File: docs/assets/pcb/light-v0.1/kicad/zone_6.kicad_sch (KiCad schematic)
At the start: 13 parts, among them J7 ZONE 6, Q116 AO3422, Q117 AO3422, Q118 AO3422

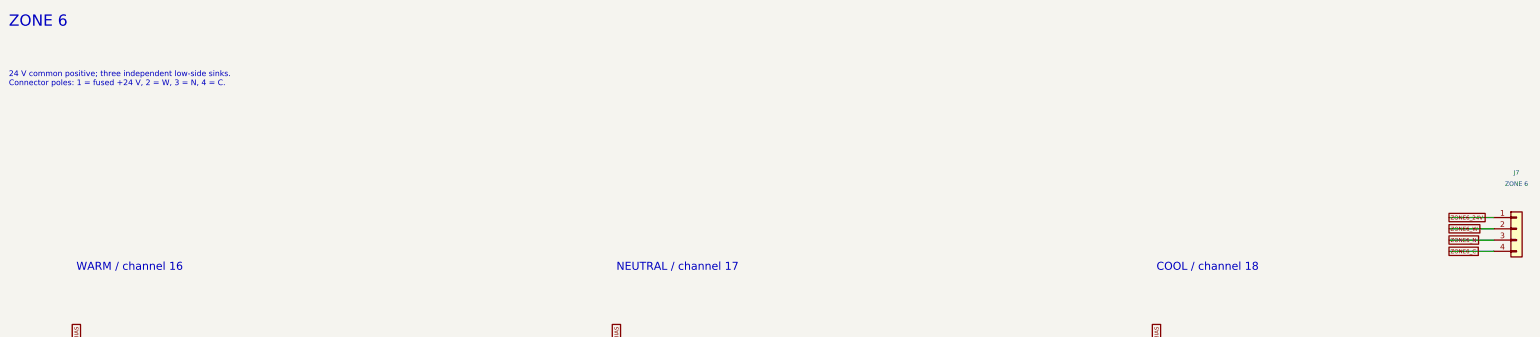
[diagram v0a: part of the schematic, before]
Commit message: Refresh PCB chapters from verified central LED snapshots
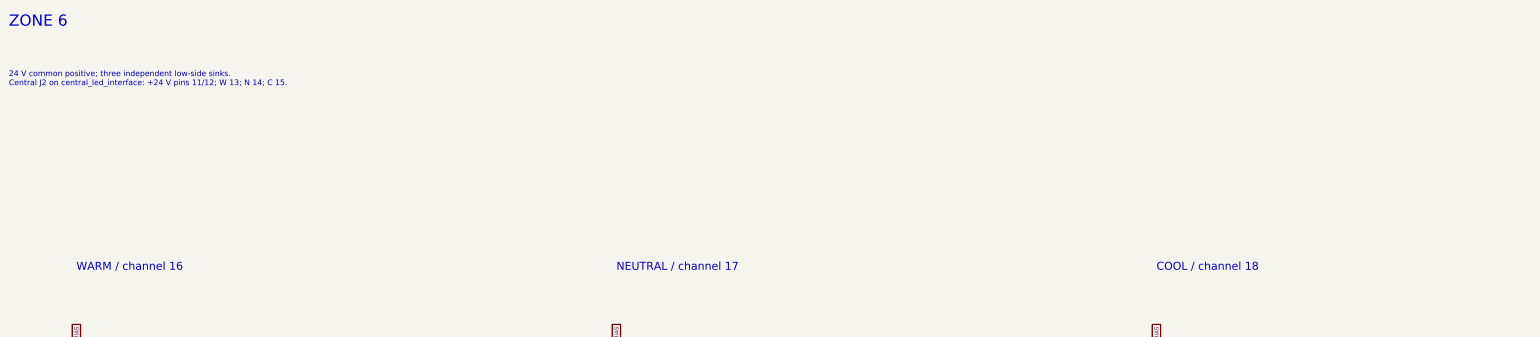
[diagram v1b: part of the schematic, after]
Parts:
- removed J7: ZONE 6, Connector_JST:JST_GH_SM04B-GHS-TB_1x04-1MP_P1.25mm_Horizontal, symbol Connector_Generic:Conn_01x04
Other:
- note added: "24 V common positive; three independent low-side sinks. Central J2 on central_led_interface: +24 V pins 11/12; W 13; N 14; C 15."
- note removed: "24 V common positive; three independent low-side sinks. Connector poles: 1 = fused +24 V, 2 = W, 3 = N, 4 = C."
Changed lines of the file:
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@@
   (title_block
     (title "Zone 6")
-    (date "2026-09-06")
-    (rev "A draft")
+    (date "2026-09-08")
+    (rev "LIGHT v0.2 candidate")
     (company "Engineered Lighting")
     (comment 1 "ENGINEERING DRAFT - see release status before fabrication"))
-  (symbol
-    (lib_id "Connector_Generic:Conn_01x04")
-    (at 360.68 63.5 0)
-    (unit 1)
-    (exclude_from_sim yes)
-    (in_bom yes)
-    (on_board yes)
-    (dnp no)
-    (property "Reference" "J7"
-      (at 360.68 50.8 0.0)
-      (effects
-        (font
-          (size 1.0 1.0))))
-    (property "Value" "ZONE 6"
-      (at 360.68 53.34 0.0)
-      (effects
-        (font
-          (size 1.0 1.0))))
-    (property "Footprint" "Connector_JST:JST_GH_SM04B-GHS-TB_1x04-1MP_P1.25mm_Horizontal"
-      (at 360.68 63.5 0.0)
-      (hide yes)
-      (effects
-        (font
-          (size 1.0 1.0))))
-    (property "MPN" "SM04B-GHS-TB(LF)(SN)"
-      (at 360.68 63.5 0.0)
-      (hide yes)
-      (effects
-        (font
-          (size 1.0 1.0))))
-    (property "Manufacturer" "JST"
-      (at 360.68 63.5 0.0)
-      (hide yes)
-      (effects
-        (font
-          (size 1.0 1.0))))
-    (property "Datasheet" ""
-      (at 360.68 63.5 0.0)
-      (hide yes)
-      (effects
-        (font
-          (size 1.0 1.0))))
-    (instances
-      (project "engineered-lighting-rev-a"
-        (path "/964013ac-cca6-5de7-b648-d598a25a58e0/7570a9f7-157b-5037-9d43-6eba1bc9ff74"
-          (reference "J7")
-          (unit 1))))
-    (pin "1"
-)
-    (pin "2"
-)
-    (pin "3"
-)
-    (pin "4"
-))
-  (wire
-    (pts
-      (xy 355.6 60.96)
-      (xy 345.44 60.96))
-    (stroke
-      (width 0)
-      (type default))
-)
-  (global_label "ZONE6_24V"
-    (shape passive)
-    (at 345.44 60.96 0.0)
-    (effects
-      (font
-        (size 0.9 0.9))
-      (justify left))
-    (property "Intersheetrefs" "${INTERSHEET_REFS}"
-      (at 345.44 60.96 0.0)
-      (hide yes)
-      (effects
-        (font
-          (size 1.0 1.0)))))
-  (wire
-    (pts
-      (xy 355.6 63.5)
-      (xy 345.44 63.5))
-    (stroke
-      (width 0)
-      (type default))
-)
-  (global_label "ZONE6_W"
-    (shape passive)
-    (at 345.44 63.5 0.0)
-    (effects
-      (font
-        (size 0.9 0.9))
-      (justify left))
-    (property "Intersheetrefs" "${INTERSHEET_REFS}"
-      (at 345.44 63.5 0.0)
-      (hide yes)
-      (effects
-        (font
-          (size 1.0 1.0)))))
-  (wire
-    (pts
-      (xy 355.6 66.04)
-      (xy 345.44 66.04))
-    (stroke
-      (width 0)
-      (type default))
-)
-  (global_label "ZONE6_N"
-    (shape passive)
-    (at 345.44 66.04 0.0)
-    (effects
-      (font
-        (size 0.9 0.9))
-      (justify left))
-    (property "Intersheetrefs" "${INTERSHEET_REFS}"
-      (at 345.44 66.04 0.0)
-      (hide yes)
-      (effects
-        (font
-          (size 1.0 1.0)))))
-  (wire
-    (pts
-      (xy 355.6 68.58)
-      (xy 345.44 68.58))
-    (stroke
-      (width 0)
-      (type default))
-)
-  (global_label "ZONE6_C"
-    (shape passive)
-    (at 345.44 68.58 0.0)
-    (effects
-      (font
-        (size 0.9 0.9))
-      (justify left))
-    (property "Intersheetrefs" "${INTERSHEET_REFS}"
-      (at 345.44 68.58 0.0)
-      (hide yes)
-      (effects
-        (font
-          (size 1.0 1.0)))))
   (symbol
     (lib_id "EL:AO3422")
@@
       (justify left top))
 )
-  (text "24 V common positive; three independent low-side sinks.\nConnector poles: 1 = fused +24 V, 2 = W, 3 = N, 4 = C."
+  (text "24 V common positive; three independent low-side sinks.\nCentral J2 on central_led_interface: +24 V pins 11/12; W 13; N 14; C 15."
     (at 20.32 27.94 0)
     (effects
